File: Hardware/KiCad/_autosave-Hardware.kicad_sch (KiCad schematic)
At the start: 1 part, among them U2 Teensy4.1

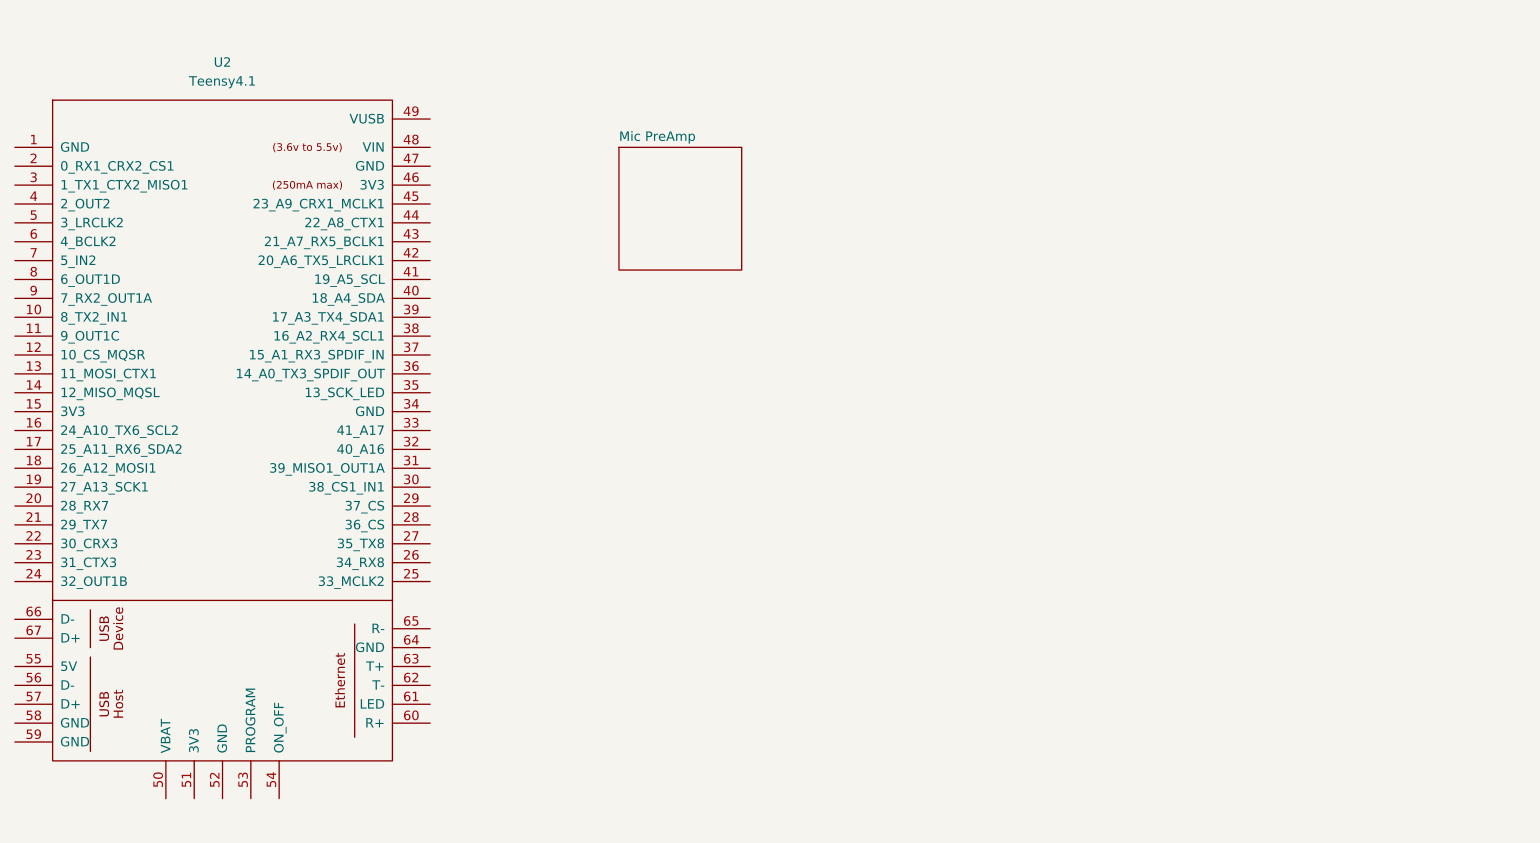
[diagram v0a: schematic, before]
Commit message: created 5V USB-C Power supply (simple version for now)
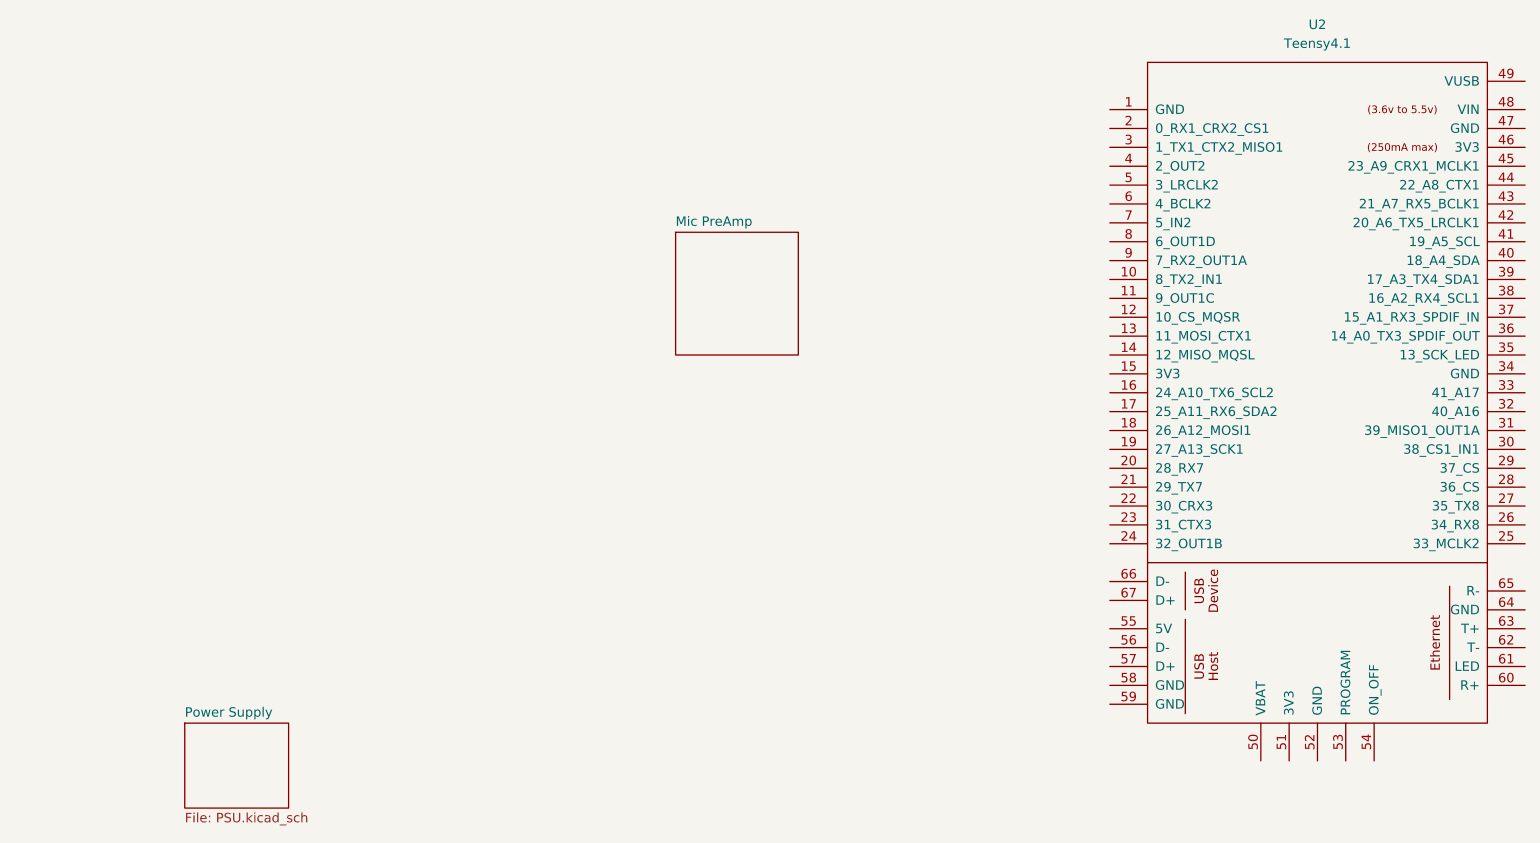
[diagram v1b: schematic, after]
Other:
- added sheet Power Supply (PSU.kicad_sch)
- moved on the sheet: U2
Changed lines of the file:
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@@
 	(symbol
 		(lib_id "Teensy:Teensy4.1")
-		(at 69.85 123.19 0)
+		(at 217.17 118.11 0)
 		(unit 1)
 		(exclude_from_sim no)
@@
 		(fields_autoplaced yes)
 		(property "Reference" "U2"
-			(at 69.85 57.15 0)
+			(at 217.17 52.07 0)
 			(effects
 				(font
@@
 		)
 		(property "Value" "Teensy4.1"
-			(at 69.85 59.69 0)
+			(at 217.17 54.61 0)
 			(effects
 				(font
@@
 		)
 		(property "Footprint" ""
-			(at 59.69 113.03 0)
+			(at 207.01 107.95 0)
 			(effects
 				(font
@@
 		)
 		(property "Datasheet" ""
-			(at 59.69 113.03 0)
+			(at 207.01 107.95 0)
 			(effects
 				(font
@@
 		)
 		(property "Description" ""
-			(at 69.85 123.19 0)
+			(at 217.17 118.11 0)
 			(effects
 				(font
@@
 	)
 	(sheet
-		(at 123.19 68.58)
+		(at 64.77 146.05)
+		(size 13.97 11.43)
+		(fields_autoplaced yes)
+		(stroke
+			(width 0.1524)
+			(type solid)
+		)
+		(fill
+			(color 0 0 0 0.0000)
+		)
+		(property "Sheetname" "Power Supply"
+			(at 64.77 145.3384 0)
+			(effects
+				(font
+					(size 1.27 1.27)
+				)
+				(justify left bottom)
+			)
+		)
+		(property "Sheetfile" "PSU.kicad_sch"
+			(at 64.77 158.0646 0)
+			(effects
+				(font
+					(size 1.27 1.27)
+				)
+				(justify left top)
+			)
+		)
+		(instances
+			(project "Hardware"
+				(path "/e827c80a-ca8d-4d24-8db6-878b575a1aed"
+					(page "3")
+				)
+			)
+		)
+	)
+	(sheet
+		(at 130.81 80.01)
 		(size 16.51 16.51)
 		(fields_autoplaced yes)
@@
 		)
 		(property "Sheetname" "Mic PreAmp"
-			(at 123.19 67.8684 0)
+			(at 130.81 79.2984 0)
 			(show_name yes)
 			(effects
@@
 		)
 		(property "Sheetfile" "PreAmp.kicad_sch"
-			(at 123.19 85.6746 0)
-			(effects
-				(font
+			(at 130.81 97.1046 0)
+			(effects
+				(font
